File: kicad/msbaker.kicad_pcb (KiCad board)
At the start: 4 copper layers, 14 x 70 mm, 37 parts, among them J1 USB_B_Micro, J2 Micro_SD_Card, J3 GPIO, U1 MIC5365-3.3YC5, U2 W25Q128JVS, U3 RP2040, U4 LSM6DSO32, Y1 12MHz

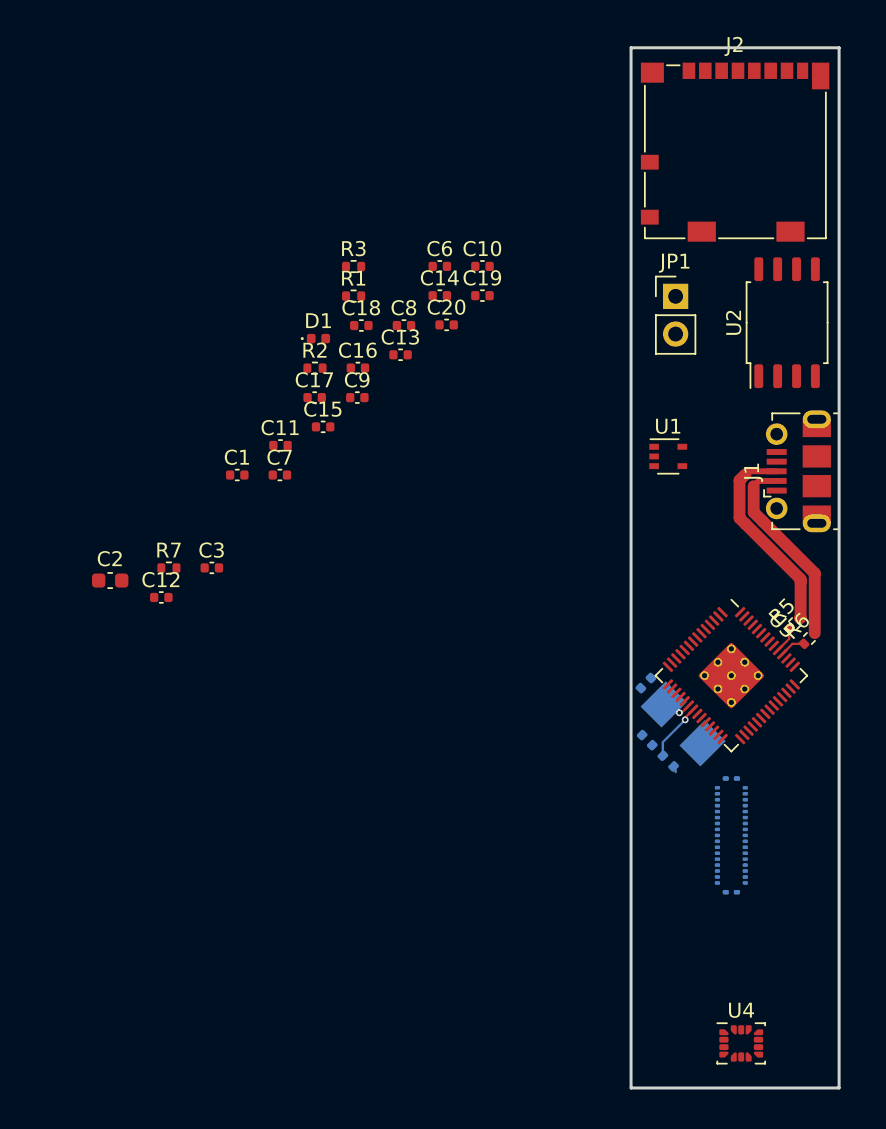
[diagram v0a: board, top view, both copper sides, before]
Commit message: Added pcb files
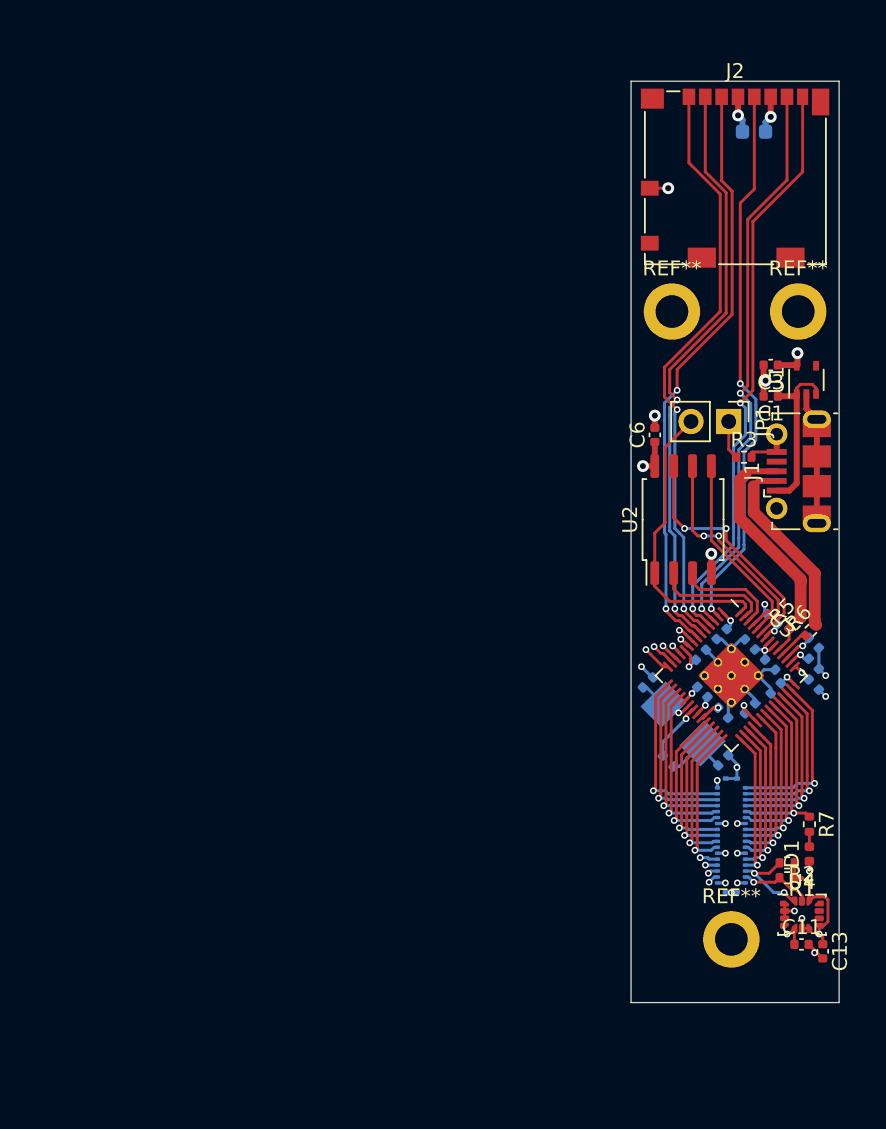
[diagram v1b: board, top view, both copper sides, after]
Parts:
- added REF**: MountingHole_2.2mm_M2_ISO14580_Pad, MountingHole:MountingHole_2.2mm_M2_ISO14580_Pad, F.Cu at (188.8, 83.0)
- added REF**: MountingHole_2.2mm_M2_ISO14580_Pad, MountingHole:MountingHole_2.2mm_M2_ISO14580_Pad, F.Cu at (180.2, 83.0)
- added REF**: MountingHole_2.2mm_M2_ISO14580_Pad, MountingHole:MountingHole_2.2mm_M2_ISO14580_Pad, F.Cu at (184.2, 125.2)
- C10, C12, C14, C15, C16, C17, C18, C19, C2, C20, C7, C8, C9: moved to B.Cu
- moved C2 52.8 mm to (185.8, 70.9)
- moved C13 49.2 mm to (190.4, 126.0), turned to -90 degrees
- moved R1 48.8 mm to (188.0, 121.1), turned to 180 degrees
- moved C11 48.5 mm to (189.0, 125.6)
- moved D1 47.9 mm to (189.5, 119.5), turned to 90 degrees
- moved R7 46.4 mm to (189.5, 117.5), turned to -90 degrees
- moved R2 46.0 mm to (188.0, 120.1), turned to 180 degrees
- moved C12 41.2 mm to (186.9, 106.8), turned to -45 degrees
- moved C3 40.0 mm to (186.9, 86.6), turned to 180 degrees
- moved C7 37.7 mm to (189.8, 105.3), turned to -45 degrees
- moved C18 37.1 mm to (187.2, 108.4), turned to -135 degrees
- moved C1 36.3 mm to (186.9, 88.7), turned to 180 degrees
- moved C17 36.0 mm to (185.5, 109.7), turned to 45 degrees
- moved C10 35.9 mm to (189.8, 108.1), turned to -45 degrees
- moved C8 33.8 mm to (183.7, 110.0), turned to -45 degrees
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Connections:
- R1 pad 2: /I2C_SCL -> /I2C0_SCL
- U3 pad 8: /I2C_SDA -> /I2C0_SDA
- U3 pad 9: /I2C_SCL -> /I2C0_SCL
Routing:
- net GND: track 0.00 -> 45.5 mm, vias 0 -> 21
- net /SD_DAT3: track 0.00 -> 39.8 mm, vias 0 -> 2
- net /SD_CMD: track 0.00 -> 39.7 mm, vias 0 -> 2
- net /SD_DAT2: track 0.00 -> 39.6 mm, vias 0 -> 2
- net /SD_DAT1: track 0.00 -> 39.5 mm, vias 0 -> 2
- net /SD_DAT0: track 0.00 -> 38.6 mm, vias 0 -> 2
- net /SD_CLK: track 0.00 -> 37.2 mm, vias 0 -> 2
- net +3.3V: track 0.00 -> 31.6 mm, vias 0 -> 14
- net /I2C0_SDA: track 0.00 -> 26.4 mm, vias 0 -> 3
- net /I2C0_SCL: track 0.00 -> 24.3 mm, vias 0 -> 2
- net Net-(JP1-Pad2): track 0.00 -> 19.4 mm
- net /GPIO8: track 0.00 -> 19.0 mm, vias 0 -> 2
- net /GPIO11: track 0.00 -> 18.8 mm, vias 0 -> 2
- net /GPIO9: track 0.00 -> 18.7 mm, vias 0 -> 2
- net /GPIO10: track 0.00 -> 18.7 mm, vias 0 -> 2
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- added copper zone on In2.Cu, net +3.3V
- added copper zone on In1.Cu, net GND
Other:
- board size 14 x 70 mm -> 14 x 62 mm

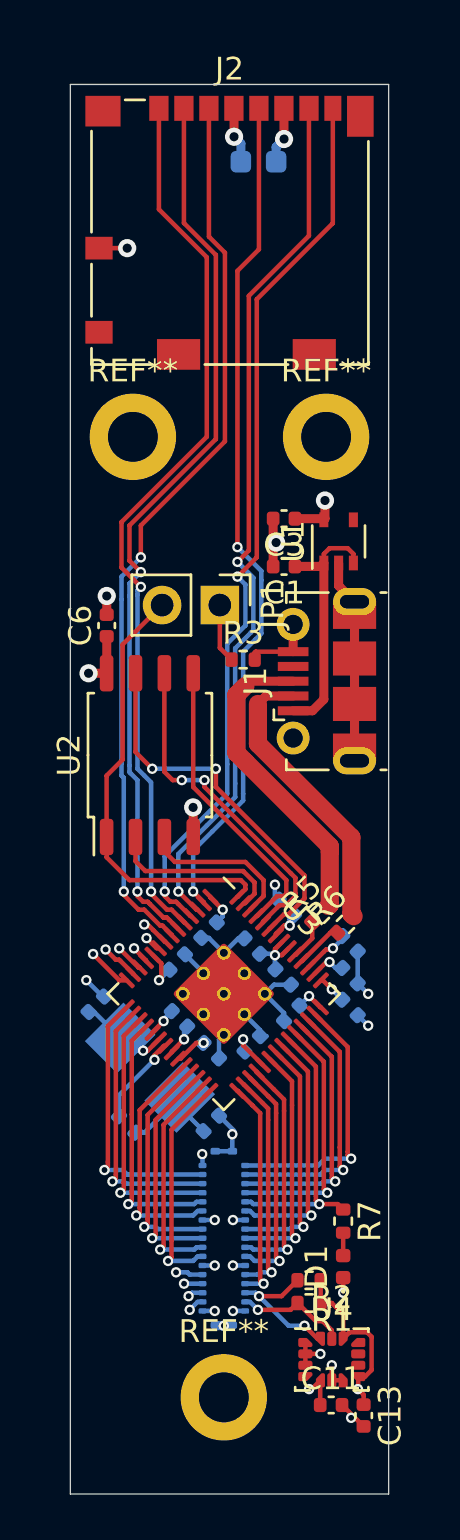
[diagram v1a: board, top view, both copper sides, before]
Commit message: Fixed references on silkscreen layer
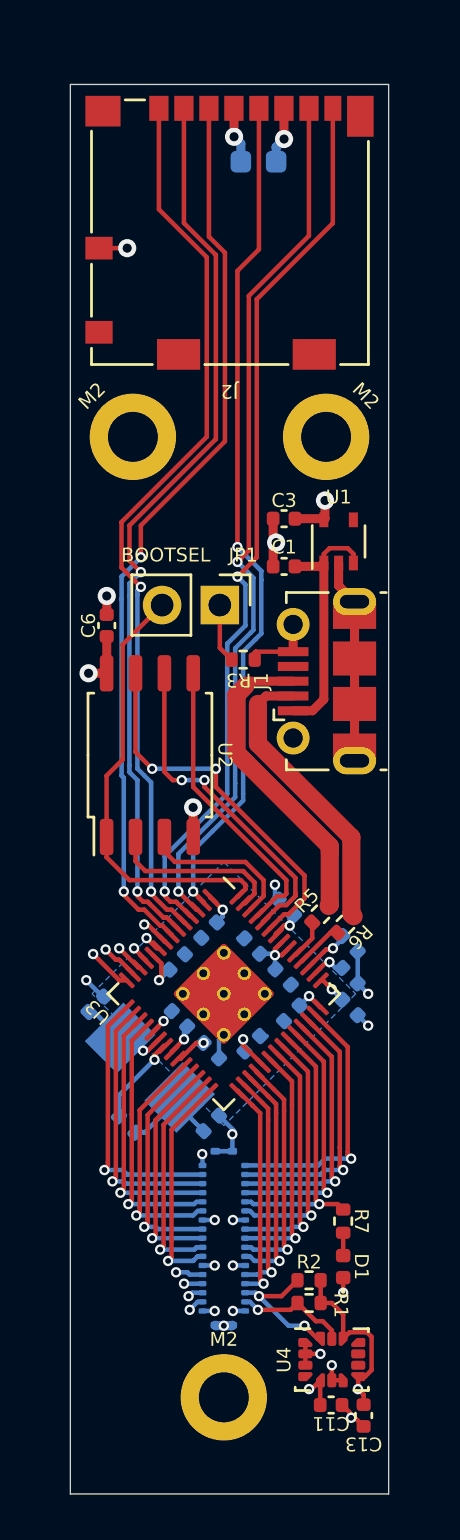
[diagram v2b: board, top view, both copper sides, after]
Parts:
- renumbered REF** to M2
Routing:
- net GND: track 45.5 -> 37.7 mm
- added copper zone on B.Cu, net GND
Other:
- board text added: "BOOTSEL"

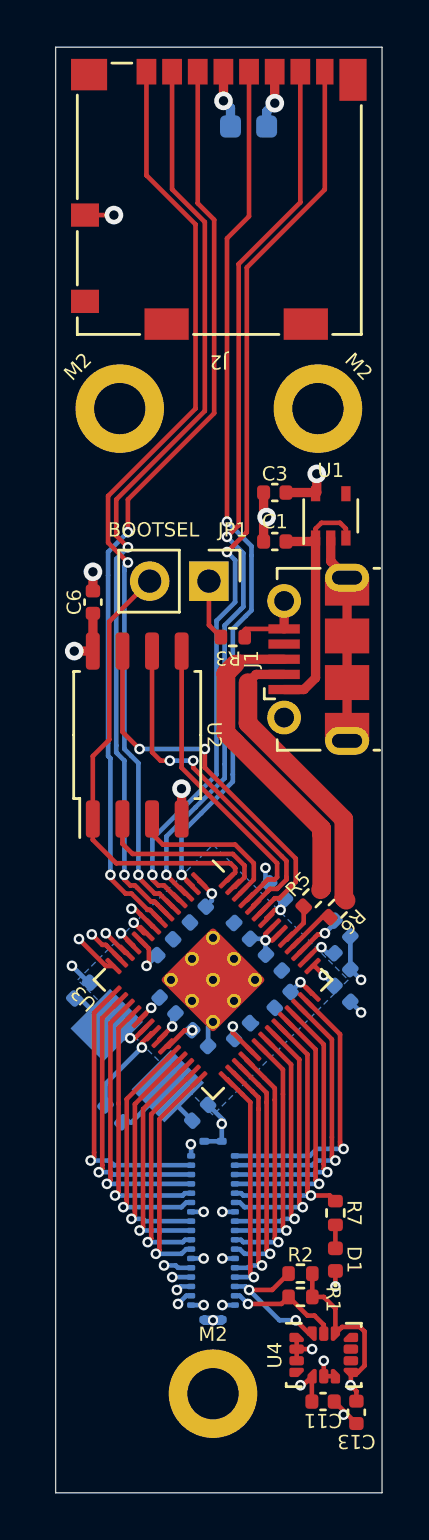
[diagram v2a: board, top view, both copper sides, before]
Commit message: Added reset jumper to PCB
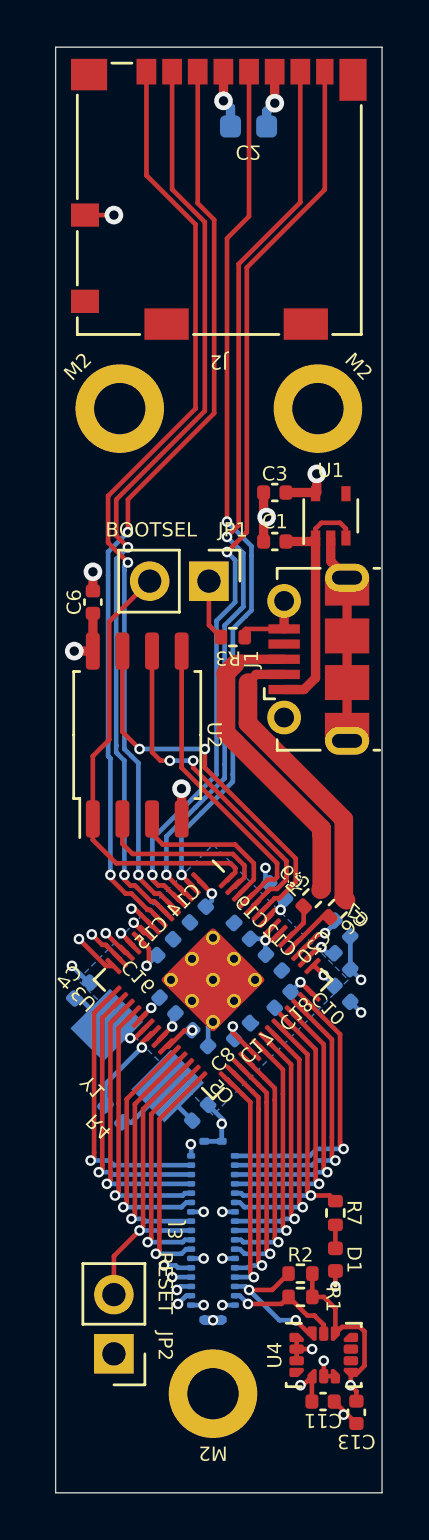
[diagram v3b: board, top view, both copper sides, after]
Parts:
- added JP2: RESET, Connector_PinHeader_2.54mm:PinHeader_1x02_P2.54mm_Vertical, F.Cu at (180.0, 123.5)
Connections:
- net Net-(JP1-Pad2) renamed /QSPI_SS
- net Net-(U2-Pad2) renamed /QSPI_SD1
- net Net-(U2-Pad3) renamed /QSPI_SD2
- net Net-(U2-Pad5) renamed /QSPI_SD0
- net Net-(U2-Pad6) renamed /QSPI_SCLK
- net Net-(U2-Pad7) renamed /QSPI_SD3
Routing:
- net /RUN: track 10.1 -> 13.3 mm
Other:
- board text removed: "BOOTSEL"
